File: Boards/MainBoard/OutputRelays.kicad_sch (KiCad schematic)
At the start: 16 parts, among them IC13 DRDNB21D-7, IC14 DRDNB21D-7, K1 AWHSH105D00G, K2 AWHSH105D00G, K3 AWHSH105D00G, K4 AWHSH105D00G

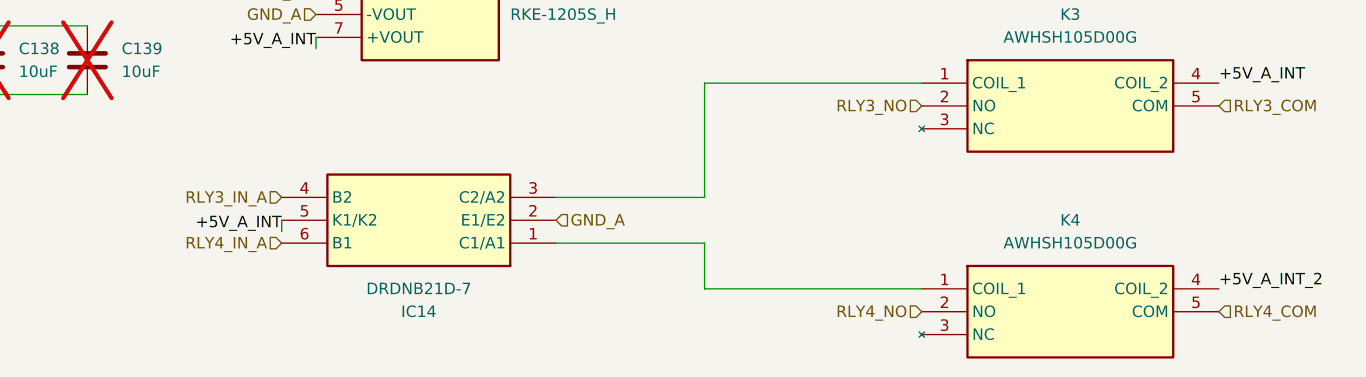
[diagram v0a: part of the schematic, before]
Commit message: Layout mainboard, add EMI filter caps
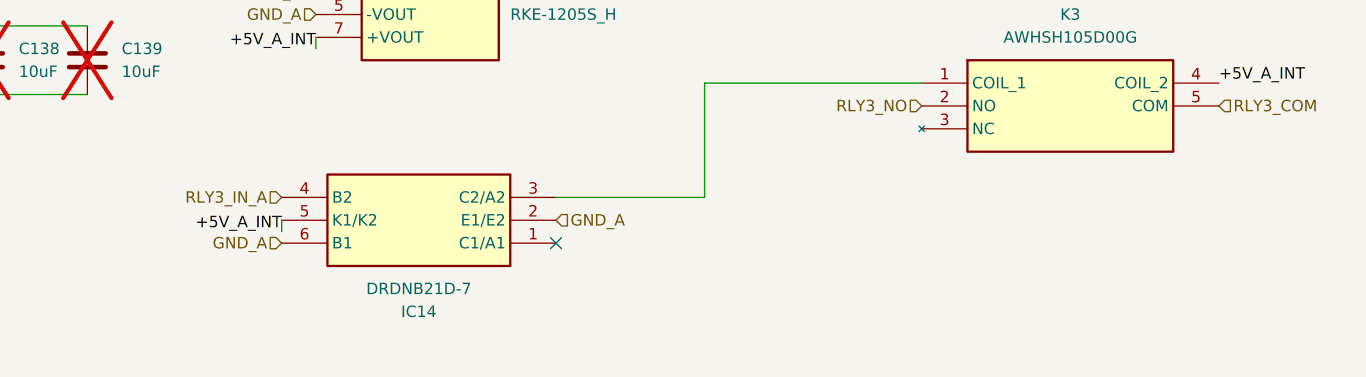
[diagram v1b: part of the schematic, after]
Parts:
- removed K4: AWHSH105D00G, InverterCom:AWHSH105D00G, symbol InverterCom:AWHSH105D00G
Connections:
- net RLY4_IN_A is gone; now on net GND_A: IC14.6 (B1)
- no-connect marks 0 -> 1
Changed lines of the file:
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@@
 		(color 0 0 0 0)
 	)
+	(no_connect
+		(at 140.97 121.92)
+	)
 	(wire
 		(pts
@@
 	(wire
 		(pts
-			(xy 157.48 127) (xy 157.48 121.92)
-		)
-		(stroke
-			(width 0)
-			(type default)
-		)
-	)
-	(wire
-		(pts
-			(xy 140.97 121.92) (xy 157.48 121.92)
-		)
-		(stroke
-			(width 0)
-			(type default)
-		)
-	)
-	(wire
-		(pts
 			(xy 78.74 46.99) (xy 90.17 46.99)
-		)
-		(stroke
-			(width 0)
-			(type default)
-		)
-	)
-	(wire
-		(pts
-			(xy 181.61 127) (xy 157.48 127)
 		)
 		(stroke
@@
 	)
 	(label "+5V_A_INT_2"
-		(at 214.63 127 0)
-		(effects
-			(font
-				(size 1.27 1.27)
-			)
-			(justify left bottom)
-		)
-	)
-	(label "+5V_A_INT_2"
 		(at 55.88 46.99 270)
 		(effects
@@
 		)
 	)
-	(hierarchical_label "RLY4_NO"
-		(shape input)
-		(at 181.61 129.54 180)
+	(hierarchical_label "GND_A"
+		(shape input)
+		(at 140.97 119.38 0)
+		(effects
+			(font
+				(size 1.27 1.27)
+			)
+			(justify left)
+		)
+	)
+	(hierarchical_label "+12V_A"
+		(shape input)
+		(at 116.84 31.75 180)
 		(effects
 			(font
@@
 		)
 	)
+	(hierarchical_label "RLY3_IN_A"
+		(shape input)
+		(at 110.49 116.84 180)
+		(effects
+			(font
+				(size 1.27 1.27)
+			)
+			(justify right)
+		)
+	)
+	(hierarchical_label "RLY1_NO"
+		(shape input)
+		(at 181.61 48.26 180)
+		(effects
+			(font
+				(size 1.27 1.27)
+			)
+			(justify right)
+		)
+	)
 	(hierarchical_label "GND_A"
 		(shape input)
-		(at 140.97 119.38 0)
+		(at 114.3 93.98 180)
+		(effects
+			(font
+				(size 1.27 1.27)
+			)
+			(justify right)
+		)
+	)
+	(hierarchical_label "RLY1_IN_A"
+		(shape input)
+		(at 110.49 58.42 180)
+		(effects
+			(font
+				(size 1.27 1.27)
+			)
+			(justify right)
+		)
+	)
+	(hierarchical_label "GND_A"
+		(shape input)
+		(at 140.97 60.96 0)
 		(effects
 			(font
@@
 		)
 	)
-	(hierarchical_label "+12V_A"
-		(shape input)
-		(at 116.84 31.75 180)
+	(hierarchical_label "RLY3_NO"
+		(shape input)
+		(at 181.61 106.68 180)
 		(effects
 			(font
@@
 		)
 	)
-	(hierarchical_label "RLY3_IN_A"
-		(shape input)
-		(at 110.49 116.84 180)
+	(hierarchical_label "GND_A"
+		(shape input)
+		(at 116.84 36.83 180)
 		(effects
 			(font
@@
 		)
 	)
-	(hierarchical_label "RLY1_NO"
-		(shape input)
-		(at 181.61 48.26 180)
+	(hierarchical_label "RLY2_IN_A"
+		(shape input)
+		(at 110.49 63.5 180)
 		(effects
 			(font
@@
 	(hierarchical_label "GND_A"
 		(shape input)
-		(at 114.3 93.98 180)
+		(at 54.61 97.79 90)
+		(effects
+			(font
+				(size 1.27 1.27)
+			)
+			(justify left)
+		)
+	)
+	(hierarchical_label "GND_A"
+		(shape input)
+		(at 114.3 96.52 180)
 		(effects
 			(font
@@
 		)
 	)
-	(hierarchical_label "RLY1_IN_A"
-		(shape input)
-		(at 110.49 58.42 180)
+	(hierarchical_label "GND_A"
+		(shape input)
+		(at 110.49 121.92 180)
 		(effects
 			(font
@@
 	(hierarchical_label "GND_A"
 		(shape input)
-		(at 140.97 60.96 0)
+		(at 55.88 39.37 90)
 		(effects
 			(font
@@
 		)
 	)
-	(hierarchical_label "RLY3_NO"
-		(shape input)
-		(at 181.61 106.68 180)
-		(effects
-			(font
-				(size 1.27 1.27)
-			)
-			(justify right)
+	(hierarchical_label "RLY2_COM"
+		(shape input)
+		(at 214.63 71.12 0)
+		(effects
+			(font
+				(size 1.27 1.27)
+			)
+			(justify left)
 		)
 	)
 	(hierarchical_label "GND_A"
 		(shape input)
-		(at 116.84 36.83 180)
-		(effects
-			(font
-				(size 1.27 1.27)
-			)
-			(justify right)
-		)
-	)
-	(hierarchical_label "RLY2_IN_A"
-		(shape input)
-		(at 110.49 63.5 180)
-		(effects
-			(font
-				(size 1.27 1.27)
-			)
-			(justify right)
-		)
-	)
-	(hierarchical_label "GND_A"
-		(shape input)
-		(at 54.61 97.79 90)
-		(effects
-			(font
-				(size 1.27 1.27)
-			)
-			(justify left)
-		)
-	)
-	(hierarchical_label "GND_A"
-		(shape input)
-		(at 114.3 96.52 180)
-		(effects
-			(font
-				(size 1.27 1.27)
-			)
-			(justify right)
-		)
-	)
-	(hierarchical_label "GND_A"
-		(shape input)
-		(at 55.88 39.37 90)
-		(effects
-			(font
-				(size 1.27 1.27)
-			)
-			(justify left)
-		)
-	)
-	(hierarchical_label "RLY2_COM"
-		(shape input)
-		(at 214.63 71.12 0)
-		(effects
-			(font
-				(size 1.27 1.27)
-			)
-			(justify left)
-		)
-	)
-	(hierarchical_label "RLY4_COM"
-		(shape input)
-		(at 214.63 129.54 0)
-		(effects
-			(font
-				(size 1.27 1.27)
-			)
-			(justify left)
-		)
-	)
-	(hierarchical_label "GND_A"
-		(shape input)
 		(at 116.84 34.29 180)
-		(effects
-			(font
-				(size 1.27 1.27)
-			)
-			(justify right)
-		)
-	)
-	(hierarchical_label "RLY4_IN_A"
-		(shape input)
-		(at 110.49 121.92 180)
 		(effects
 			(font
@@
 					(unit 1)
 				)
-			)
-		)
-	)
-	(symbol
-		(lib_id "InverterCom:AWHSH105D00G")
-		(at 181.61 127 0)
-		(unit 1)
-		(exclude_from_sim no)
-		(in_bom yes)
-		(on_board yes)
-		(dnp no)
-		(fields_autoplaced yes)
-		(property "Reference" "K4"
-			(at 198.12 119.38 0)
-			(effects
-				(font
-					(size 1.27 1.27)
-				)
-			)
-		)
-		(property "Value" "AWHSH105D00G"
-			(at 198.12 121.92 0)
-			(effects
-				(font
-					(size 1.27 1.27)
-				)
-			)
-		)
-		(property "Footprint" "InverterCom:AWHSH105D00G"
-			(at 210.82 221.92 0)
-			(effects
-				(font
-					(size 1.27 1.27)
-				)
-				(justify left top)
-				(hide yes)
-			)
-		)
-		(property "Datasheet" "https://g.componentsearchengine.com/Datasheets/0/17861032.pdf"
-			(at 210.82 321.92 0)
-			(effects
-				(font
-					(size 1.27 1.27)
-				)
-				(justify left top)
-				(hide yes)
-			)
-		)
-		(property "Description" "General Purpose Relays Commercial RelayRated Carrying Current :15AType of Sealing : Sealed and Waterproof TypeNumber of pole : one poleCoil Voltage : 5VCoil Type : Standard DC CoilContact Form : Form C"
-			(at 181.61 127 0)
-			(effects
-				(font
-					(size 1.27 1.27)
-				)
-				(hide yes)
-			)
-		)
-		(property "Height" "15.3"
-			(at 210.82 521.92 0)
-			(effects
-				(font
-					(size 1.27 1.27)
-				)
-				(justify left top)
-				(hide yes)
-			)
-		)
-		(property "Mouser Part Number" "523-AWHSH105D00G"
-			(at 210.82 621.92 0)
-			(effects
-				(font
-					(size 1.27 1.27)
-				)
-				(justify left top)
-				(hide yes)
-			)
-		)
-		(property "Mouser Price/Stock" "https://www.mouser.co.uk/ProductDetail/Amphenol-Anytek/AWHSH105D00G?qs=rSMjJ%252B1ewcT7jFUGTuCYSw%3D%3D"
-			(at 210.82 721.92 0)
-			(effects
-				(font
-					(size 1.27 1.27)
-				)
-				(justify left top)
-				(hide yes)
-			)
-		)
-		(property "Manufacturer_Name" "Amphenol"
-			(at 210.82 821.92 0)
-			(effects
-				(font
-					(size 1.27 1.27)
-				)
-				(justify left top)
-				(hide yes)
-			)
-		)
-		(property "Manufacturer_Part_Number" "AWHSH105D00G"
-			(at 210.82 921.92 0)
-			(effects
-				(font
-					(size 1.27 1.27)
-				)
-				(justify left top)
-				(hide yes)
-			)
-		)
-		(pin "4"
-		)
-		(pin "1"
-		)
-		(pin "5"
-		)
-		(pin "2"
-		)
-		(pin "3"
-		)
-		(instances
-			(project "MainBoard"
-				(path "/1bd20b11-4068-4af7-8516-b3d686707223/3f1e0dfd-3bb5-4a06-942c-ceeb344b0f52"
-					(reference "K4")
-					(unit 1)
-				)
